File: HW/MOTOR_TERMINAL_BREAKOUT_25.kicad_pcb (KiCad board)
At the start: 2 copper layers, 30.4 x 25 mm, 9 parts

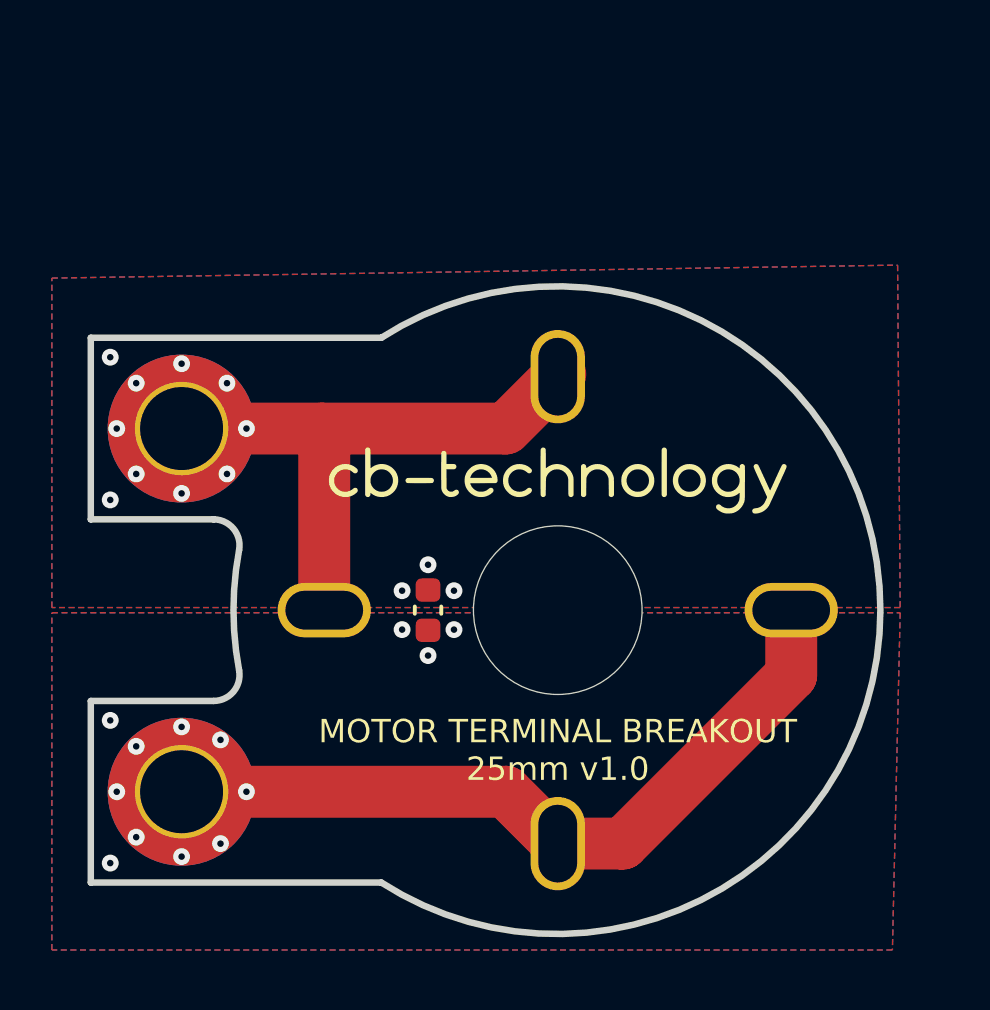
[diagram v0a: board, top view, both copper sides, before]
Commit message: Make Minor Updates to Mount Holes and Silkscreen
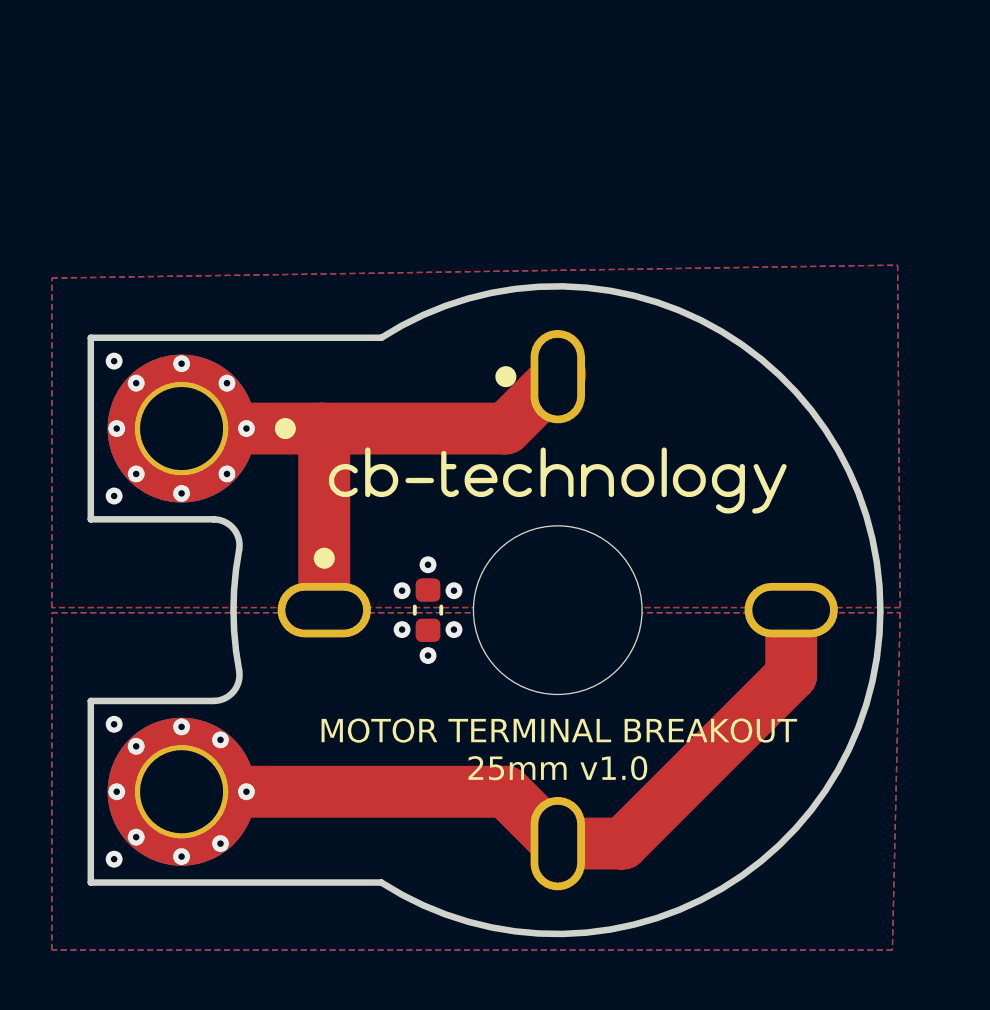
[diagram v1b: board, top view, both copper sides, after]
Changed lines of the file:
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@@
     )
   )
-  (gr_rect (start 202.25 139.75) (end 205.5 146.25) (layer "B.Mask") (width 0.1) (fill solid))
-  (gr_circle (center 205.5 143) (end 208.75 143) (layer "B.Mask") (width 0.1) (fill solid))
-  (gr_rect (start 202.25 153.75) (end 205.5 160.25) (layer "B.Mask") (width 0.1) (fill solid))
-  (gr_circle (center 205.5 157) (end 208.75 157) (layer "B.Mask") (width 0.1) (fill solid))
-  (gr_rect (start 202.25 139.75) (end 205.5 146.25) (layer "F.Mask") (width 0.1) (fill solid))
-  (gr_circle (center 205.5 143) (end 208.75 143) (layer "F.Mask") (width 0.1) (fill solid))
-  (gr_circle (center 205.5 157) (end 208.75 157) (layer "F.Mask") (width 0.1) (fill solid))
-  (gr_rect (start 202.25 153.75) (end 205.5 160.25) (layer "F.Mask") (width 0.1) (fill solid))
+  (gr_circle (center 211 148) (end 211.4 148) (layer "F.SilkS") (width 0.01) (fill solid))
+  (gr_circle (center 218 141) (end 218.4 141) (layer "F.SilkS") (width 0.01) (fill solid))
+  (gr_circle (center 209.5 143) (end 209.9 143) (layer "F.SilkS") (width 0.01) (fill solid))
+  (gr_rect (start 202.5 140) (end 205.5 146) (layer "B.Mask") (width 0.1) (fill solid))
+  (gr_circle (center 205.5 143) (end 208.5 143) (layer "B.Mask") (width 0.1) (fill solid))
+  (gr_rect (start 202.5 154) (end 205.5 160) (layer "B.Mask") (width 0.1) (fill solid))
+  (gr_circle (center 205.5 157) (end 208.5 157) (layer "B.Mask") (width 0.1) (fill solid))
+  (gr_rect (start 202.5 140) (end 205.5 146) (layer "F.Mask") (width 0.1) (fill solid))
+  (gr_circle (center 205.5 143) (end 208.5 143) (layer "F.Mask") (width 0.1) (fill solid))
+  (gr_circle (center 205.5 157) (end 208.5 157) (layer "F.Mask") (width 0.1) (fill solid))
+  (gr_rect (start 202.5 154) (end 205.5 160) (layer "F.Mask") (width 0.1) (fill solid))
   (gr_line locked (start 202 153.5) (end 202 160.5) (layer "Edge.Cuts") (width 0.25))
   (gr_arc locked (start 206.733501 146.5) (mid 207.503301 146.861715) (end 207.716204 147.685185) (layer "Edge.Cuts") (width 0.25))
@@
   (segment (start 229 150) (end 229 152.5) (width 2) (layer "F.Cu") (net 1))
   (via (at 203.75 155.25) (size 0.65) (drill 0.25) (layers "F.Cu" "B.Cu") (free) (net 1))
-  (via (at 202.75 159.75) (size 0.65) (drill 0.25) (layers "F.Cu" "B.Cu") (free) (net 1))
+  (via (at 202.9 159.6) (size 0.65) (drill 0.25) (layers "F.Cu" "B.Cu") (free) (net 1))
   (via (at 215 151.75) (size 0.65) (drill 0.25) (layers "F.Cu" "B.Cu") (free) (net 1))
   (via (at 205.5 159.5) (size 0.65) (drill 0.25) (layers "F.Cu" "B.Cu") (free) (net 1))
@@
   (via (at 203 157) (size 0.65) (drill 0.25) (layers "F.Cu" "B.Cu") (free) (net 1))
   (via (at 205.5 154.5) (size 0.65) (drill 0.25) (layers "F.Cu" "B.Cu") (free) (net 1))
-  (via (at 202.75 154.25) (size 0.65) (drill 0.25) (layers "F.Cu" "B.Cu") (free) (net 1))
+  (via (at 202.9 154.4) (size 0.65) (drill 0.25) (layers "F.Cu" "B.Cu") (free) (net 1))
   (via (at 207 159) (size 0.65) (drill 0.25) (layers "F.Cu" "B.Cu") (free) (net 1))
   (via (at 214 150.75) (size 0.65) (drill 0.25) (layers "F.Cu" "B.Cu") (free) (net 1))
@@
   (via (at 205.5 145.5) (size 0.65) (drill 0.25) (layers "F.Cu" "B.Cu") (free) (net 2))
   (via (at 207.25 144.75) (size 0.65) (drill 0.25) (layers "F.Cu" "B.Cu") (free) (net 2))
-  (via (at 202.75 140.25) (size 0.65) (drill 0.25) (layers "F.Cu" "B.Cu") (free) (net 2))
+  (via (at 202.9 140.4) (size 0.65) (drill 0.25) (layers "F.Cu" "B.Cu") (free) (net 2))
   (via (at 203 143) (size 0.65) (drill 0.25) (layers "F.Cu" "B.Cu") (free) (net 2))
   (via (at 214 149.25) (size 0.65) (drill 0.25) (layers "F.Cu" "B.Cu") (free) (net 2))
@@
   (via (at 215 148.25) (size 0.65) (drill 0.25) (layers "F.Cu" "B.Cu") (free) (net 2))
   (via (at 203.75 144.75) (size 0.65) (drill 0.25) (layers "F.Cu" "B.Cu") (free) (net 2))
-  (via (at 202.75 145.75) (size 0.65) (drill 0.25) (layers "F.Cu" "B.Cu") (free) (net 2))
+  (via (at 202.9 145.6) (size 0.65) (drill 0.25) (layers "F.Cu" "B.Cu") (free) (net 2))
   (zone (net 1) (net_name "GND") (layers F&B.Cu) (hatch edge 0.508)
     (connect_pads yes (clearance 0.2))

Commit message: Adjust Hole Positions to Account For Terminal Angle on Motor
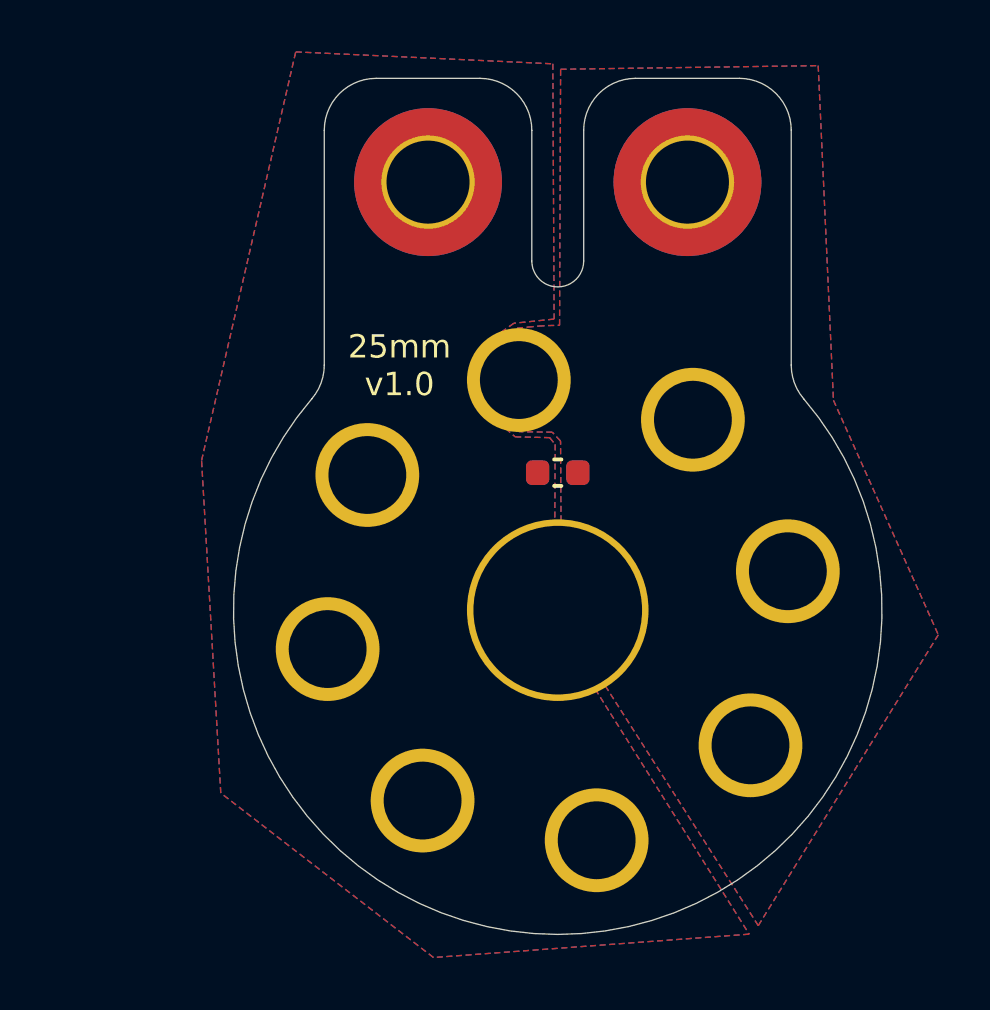
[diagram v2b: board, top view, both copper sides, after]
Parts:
- removed G***: LOGO, LOGO
- removed H12: MountingHole_Pad, MountingHole:MountingHole_3.2mm_M3_ISO7380_Pad_TopBottom
- added H10: MountingHole_Pad, MountingHole:MountingHole_3mm_Pad_TopBottom, F.Cu at (212.7, 144.8)
- added H4: MountingHole_Pad, MountingHole:MountingHole_3mm_Pad_TopBottom, F.Cu at (211.1, 151.5)
- added H7: MountingHole_Pad, MountingHole:MountingHole_3mm_Pad_TopBottom, F.Cu at (225.2, 142.7)
- added H8: MountingHole_Pad, MountingHole:MountingHole_3mm_Pad_TopBottom, F.Cu at (221.5, 158.9)
- added H9: MountingHole_Pad, MountingHole:MountingHole_3mm_Pad_TopBottom, F.Cu at (228.9, 148.5)
- H3, H5, H6: footprint MountingHole:MountingHole_3.2mm_M3_ISO7380_Pad_TopBottom -> MountingHole:MountingHole_3mm_Pad_TopBottom
- moved H2 25.3 mm to (215.0, 133.5)
- moved H1 21.7 mm to (225.0, 133.5)
- moved H3 16.0 mm to (227.4, 155.2)
- moved H5 11.6 mm to (218.5, 141.1), turned to 0 degrees
- moved C1 7.29 mm to (220.0, 144.7), turned to 180 degrees
- moved H6 5.47 mm to (214.8, 157.3)
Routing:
- net GND: track 29.5 -> 0.00 mm, vias 13 -> 0
- net +BATT: track 22.3 -> 0.00 mm, vias 13 -> 0
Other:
- board size 30.4 x 25 mm -> 25 x 33 mm
- board text added: "25mm v1.0"
- board text removed: "MOTOR TERMINAL BREAKOUT 25mm v1.0"
